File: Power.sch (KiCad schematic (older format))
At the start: 17 parts, among them U301 AOZ6605PI-1

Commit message: Updating loop compensation values with asperational attempt.
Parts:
- C310: value DNF -> 2nF; Description CAP CER 0.1UF 50V X7R 0603 -> CAP CER 0.1nF 50V X7R 0603
- R302: value DNF -> 50k
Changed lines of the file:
@@
 P 6250 3300
 F 0 "R302" H 6182 3254 50  0000 R CNN
-F 1 "DNF" H 6182 3345 50  0000 R CNN
+F 1 "50k" H 6182 3345 50  0000 R CNN
 F 2 "Resistor_SMD:R_0603_1608Metric_Pad1.05x0.95mm_HandSolder" H 6250 3300 50  0001 C CNN
 F 3 "~" H 6250 3300 50  0001 C CNN
@@
 AR Path="/5DA95EB0/5DBFE1F7" Ref="C310"  Part="1"
 F 0 "C310" H 6365 3646 50  0000 L CNN
-F 1 "DNF" H 6365 3555 50  0000 L CNN
+F 1 "2nF" H 6365 3555 50  0000 L CNN
 F 2 "Capacitor_SMD:C_0603_1608Metric_Pad1.05x0.95mm_HandSolder" H 6288 3450 50  0001 C CNN
 F 3 "~" H 6250 3600 50  0001 C CNN
 F 4 "0603" H 6150 3700 50  0000 L TNN "Package"
-F 5 "CAP CER 0.1UF 50V X7R 0603" H 6250 3600 50  0001 C CNN "Description"
+F 5 "CAP CER 0.1nF 50V X7R 0603" H 6250 3600 50  0001 C CNN "Description"
 F 6 "50V" H 6250 3550 50  0000 R TNN "Voltage Rating"
 F 7 "https://www.digikey.com/product-detail/en/samsung-electro-mechanics/CL10B104KB8NNNC/1276-1000-1-ND/3889086" H 6250 3600 50  0001 C CNN "Link"

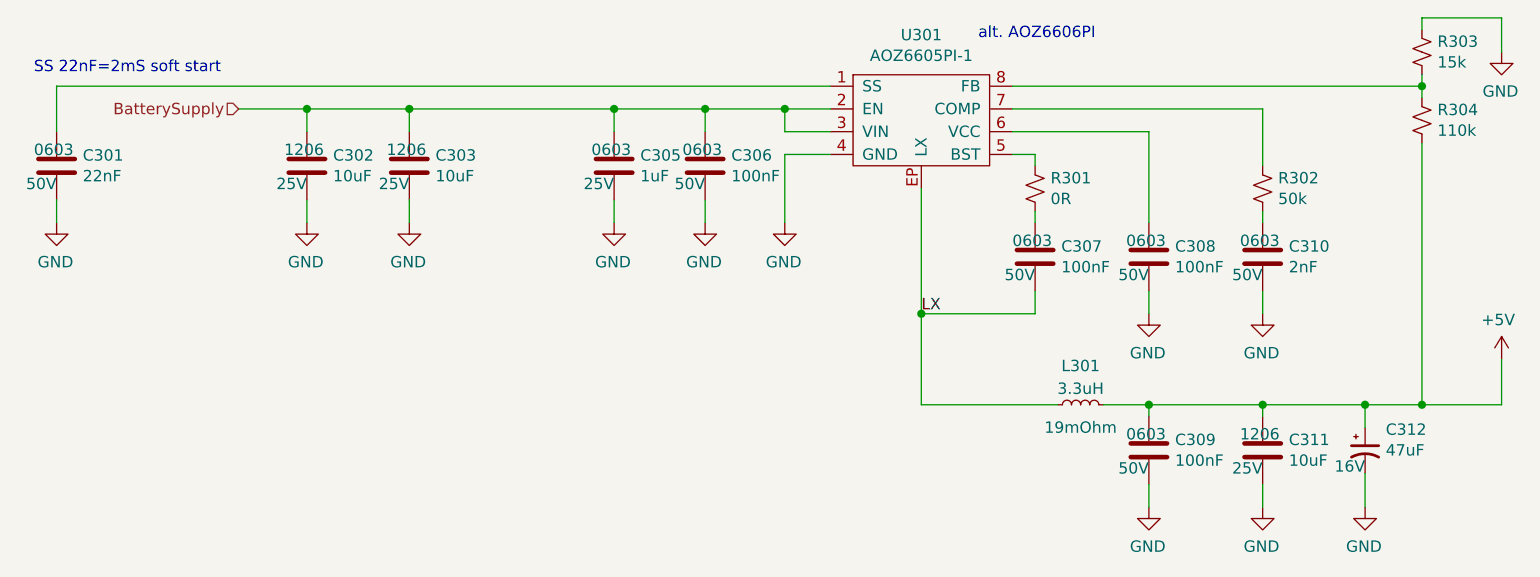
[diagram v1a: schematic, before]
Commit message: Flipping IMU to back of board.
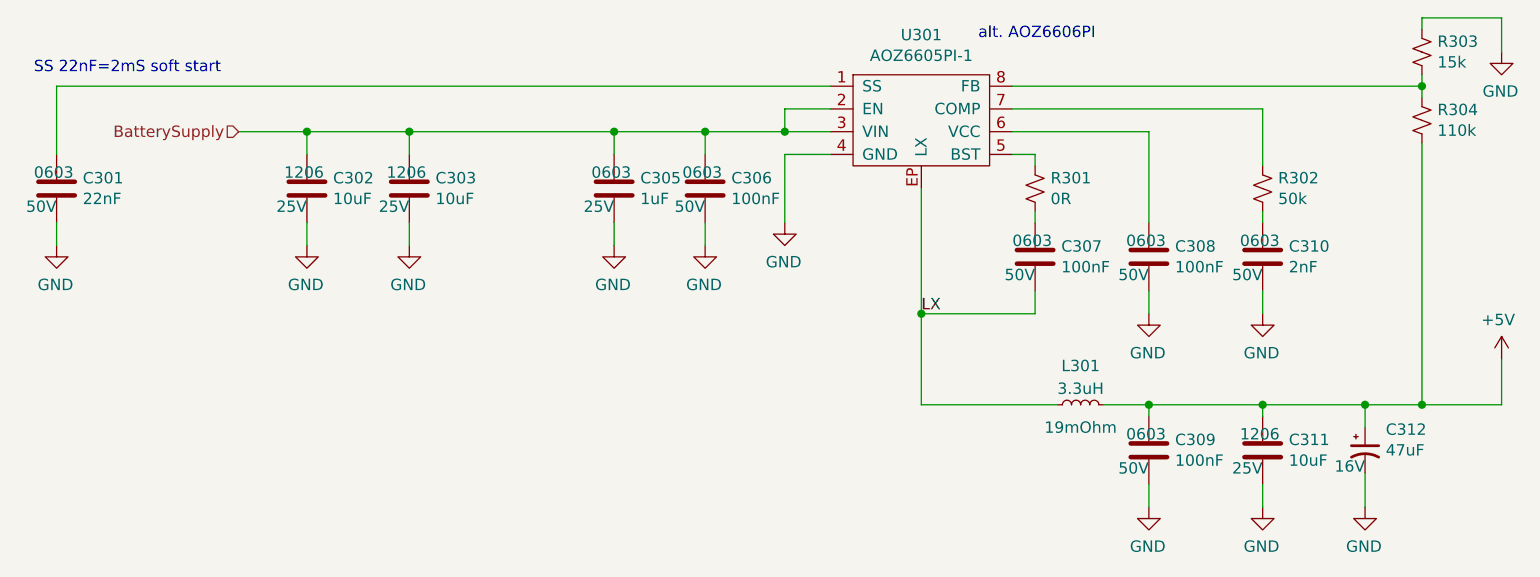
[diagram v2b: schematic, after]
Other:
- moved on the sheet: C301, C302, C303, C305, C306
